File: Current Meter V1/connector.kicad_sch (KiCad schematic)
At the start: 3 parts, among them J501 Connector

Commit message: sheet organization and microcontroller updated
organized schematic into hierarchical sheets and updated pins on microcontroller
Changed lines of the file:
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@@
 	)
 	(hierarchical_label "VBATT+"
-		(shape input)
+		(shape output)
 		(at 107.95 71.12 0)
 		(effects
@@
 		(instances
 			(project "CMU - Current Measurement Unit"
-				(path "/a2a38fd0-928e-4aba-88ec-c7bc808fdbf7/19b12faf-7b71-46cf-92b2-c5966ba55c9d/8ea9aa4f-76bf-41e8-b637-3d0ffab80390"
+				(path "/a2a38fd0-928e-4aba-88ec-c7bc808fdbf7/42f9ebbf-a8dd-474a-8f3f-d64743029b95"
 					(reference "J501")
 					(unit 1)
@@
 		(instances
 			(project "CMU - Current Measurement Unit"
-				(path "/a2a38fd0-928e-4aba-88ec-c7bc808fdbf7/19b12faf-7b71-46cf-92b2-c5966ba55c9d/8ea9aa4f-76bf-41e8-b637-3d0ffab80390"
+				(path "/a2a38fd0-928e-4aba-88ec-c7bc808fdbf7/42f9ebbf-a8dd-474a-8f3f-d64743029b95"
 					(reference "C502")
 					(unit 1)
@@
 		(instances
 			(project "CMU - Current Measurement Unit"
-				(path "/a2a38fd0-928e-4aba-88ec-c7bc808fdbf7/19b12faf-7b71-46cf-92b2-c5966ba55c9d/8ea9aa4f-76bf-41e8-b637-3d0ffab80390"
+				(path "/a2a38fd0-928e-4aba-88ec-c7bc808fdbf7/42f9ebbf-a8dd-474a-8f3f-d64743029b95"
 					(reference "C501")
 					(unit 1)
@@
 		(instances
 			(project "CMU - Current Measurement Unit"
-				(path "/a2a38fd0-928e-4aba-88ec-c7bc808fdbf7/19b12faf-7b71-46cf-92b2-c5966ba55c9d/8ea9aa4f-76bf-41e8-b637-3d0ffab80390"
+				(path "/a2a38fd0-928e-4aba-88ec-c7bc808fdbf7/42f9ebbf-a8dd-474a-8f3f-d64743029b95"
 					(reference "#PWR0501")
 					(unit 1)

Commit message: microcontroller update
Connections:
- net VBATT+ renamed +5_V
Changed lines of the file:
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@@
 		)
 	)
-	(hierarchical_label "VBATT+"
+	(hierarchical_label "+5_V"
 		(shape output)
 		(at 107.95 71.12 0)

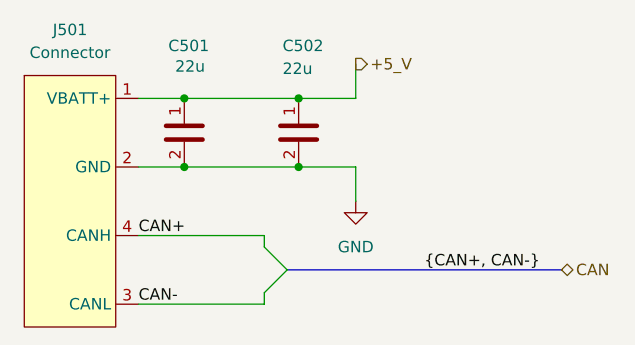
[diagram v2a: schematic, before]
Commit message: updated footprints
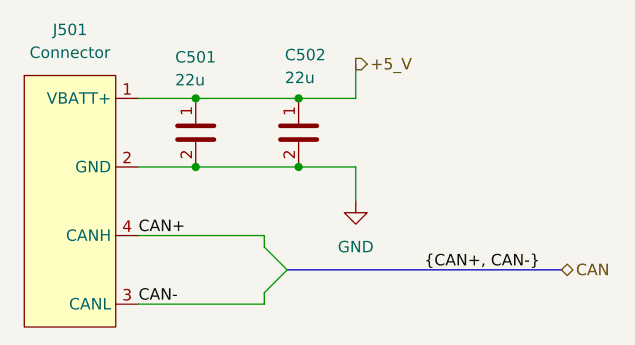
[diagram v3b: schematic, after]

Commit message: updated layout
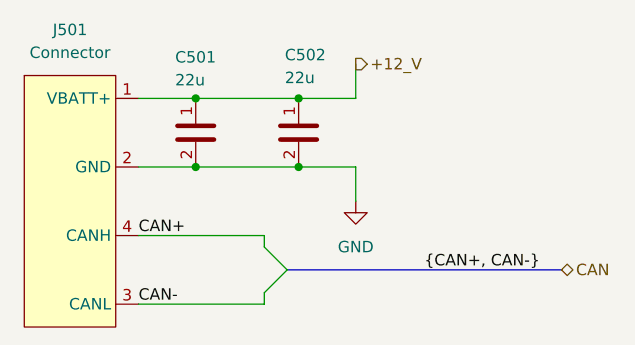
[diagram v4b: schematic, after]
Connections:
- net +5_V renamed +12_V
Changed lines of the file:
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@@
 		)
 	)
-	(hierarchical_label "+5_V"
+	(hierarchical_label "+12_V"
 		(shape output)
 		(at 107.95 71.12 0)
